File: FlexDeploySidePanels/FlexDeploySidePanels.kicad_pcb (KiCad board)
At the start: 2 copper layers, 411.4 x 215.5 mm, 0 parts

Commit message: added solar panels to layout
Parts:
- added H1: MountingHole_Pad, MountingHole:MountingHole_2.2mm_M2_DIN965_Pad_TopBottom, F.Cu at (839.4, 69.7)
- added H2: MountingHole_Pad, MountingHole:MountingHole_2.2mm_M2_DIN965_Pad_TopBottom, F.Cu at (839.4, 75.1)
- added H3: MountingHole_Pad, MountingHole:MountingHole_2.2mm_M2_DIN965_Pad_TopBottom, F.Cu at (839.4, 80.4)
- added H4: MountingHole_Pad, MountingHole:MountingHole_2.2mm_M2_DIN965_Pad_TopBottom, F.Cu at (839.4, 85.8)
- added SC1: ~, FlexDeploySidePanels:SM141K08TFV, F.Cu at (628.4, 82.2)
- added SC10: ~, FlexDeploySidePanels:SM141K08TFV, F.Cu at (674.7, 112.5)
- added SC11: ~, FlexDeploySidePanels:SM141K08TFV, F.Cu at (674.7, 142.8)
- added SC12: ~, FlexDeploySidePanels:SM141K08TFV, F.Cu at (674.7, 173.1)
- added SC13: ~, FlexDeploySidePanels:SM141K08TFV, F.Cu at (674.7, 203.4)
- added SC14: ~, FlexDeploySidePanels:SM141K08TFV, F.Cu at (674.7, 233.7)
- added SC15: ~, FlexDeploySidePanels:SM141K08TFV, F.Cu at (674.7, 264.0)
- added SC16: ~, FlexDeploySidePanels:SM141K08TFV, F.Cu at (674.7, 294.3)
- added SC17: ~, FlexDeploySidePanels:SM141K08TFV, F.Cu at (721.0, 82.2)
- added SC18: ~, FlexDeploySidePanels:SM141K08TFV, F.Cu at (721.0, 112.5)
- added SC19: ~, FlexDeploySidePanels:SM141K08TFV, F.Cu at (721.0, 142.8)
- added SC2: ~, FlexDeploySidePanels:SM141K08TFV, F.Cu at (628.4, 112.5)
- added SC20: ~, FlexDeploySidePanels:SM141K08TFV, F.Cu at (721.0, 173.1)
- added SC21: ~, FlexDeploySidePanels:SM141K08TFV, F.Cu at (721.0, 203.4)
- added SC22: ~, FlexDeploySidePanels:SM141K08TFV, F.Cu at (721.0, 233.7)
- added SC23: ~, FlexDeploySidePanels:SM141K08TFV, F.Cu at (721.0, 264.0)
- added SC24: ~, FlexDeploySidePanels:SM141K08TFV, F.Cu at (721.0, 294.3)
- added SC25: ~, FlexDeploySidePanels:SM141K08TFV, F.Cu at (767.3, 82.2)
- added SC26: ~, FlexDeploySidePanels:SM141K08TFV, F.Cu at (767.3, 112.5)
- added SC27: ~, FlexDeploySidePanels:SM141K08TFV, F.Cu at (767.3, 142.8)
- added SC28: ~, FlexDeploySidePanels:SM141K08TFV, F.Cu at (767.3, 173.1)
- added SC29: ~, FlexDeploySidePanels:SM141K08TFV, F.Cu at (767.3, 203.4)
- added SC3: ~, FlexDeploySidePanels:SM141K08TFV, F.Cu at (628.4, 142.8)
- added SC30: ~, FlexDeploySidePanels:SM141K08TFV, F.Cu at (767.3, 233.7)
- added SC31: ~, FlexDeploySidePanels:SM141K08TFV, F.Cu at (767.3, 264.0)
- added SC32: ~, FlexDeploySidePanels:SM141K08TFV, F.Cu at (767.3, 294.3)
- added SC33: ~, FlexDeploySidePanels:SM141K08TFV, F.Cu at (813.6, 82.2)
- added SC34: ~, FlexDeploySidePanels:SM141K08TFV, F.Cu at (813.6, 112.5)
- added SC35: ~, FlexDeploySidePanels:SM141K08TFV, F.Cu at (813.6, 142.8)
- added SC36: ~, FlexDeploySidePanels:SM141K08TFV, F.Cu at (813.6, 173.1)
- added SC37: ~, FlexDeploySidePanels:SM141K08TFV, F.Cu at (813.6, 203.4)
- added SC38: ~, FlexDeploySidePanels:SM141K08TFV, F.Cu at (813.6, 233.7)
- added SC4: ~, FlexDeploySidePanels:SM141K08TFV, F.Cu at (628.4, 173.1)
- added SC5: ~, FlexDeploySidePanels:SM141K08TFV, F.Cu at (628.4, 203.4)
- added SC6: ~, FlexDeploySidePanels:SM141K08TFV, F.Cu at (628.4, 233.7)
- added SC7: ~, FlexDeploySidePanels:SM141K08TFV, F.Cu at (628.4, 264.0)
- added SC8: ~, FlexDeploySidePanels:SM141K08TFV, F.Cu at (628.4, 294.3)
- added SC9: ~, FlexDeploySidePanels:SM141K08TFV, F.Cu at (674.7, 82.2)

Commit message: updated edge cuts
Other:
- board outline removed

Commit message: First rev of the full schematic and layout (very rough)
My traces are shit bc I don't know how to draw traces properly.
I didn't do the diode traces because I was struggling with vias.
The diodes should probably be moved bc I wasn't sure where was best to place them for ideal trace drawing.
I think we should have multiple traces of vsolar and gnd that cross each of the bends.
Multiple traces instead of one large one to prevent crack propagation. Better yet: multiple large ones.
Any copper in the bends should run perpendicular to the bending axis per manufacturer recommendations.
I made through hole pads for the mounting holes, but didn't place them in the right spots in the layout. The mounting holes are not at nice intervals in the CAD for good reason, but the kicad grid snap wasn't cutting it.
The cells are also not precisely placed. They are like +-2 mm or so, but they don't all line up perfectly which must change, for I am seriously irked by it. Now I know why nobody's board holes line up properly: they just put them in random spots near where they should be :skull:. Is there a way to position components by offsetting it from things by a float value (like dimension tool in CAD)?
Each panel has 8 cells in series. All panels are in parallel. We might find out from testing that we need to remove another cell from the body-fixed panel for the camera to freely glide out. In this case, we can put 9 cells on another panel :shrug::skin-tone-6:.
The camera mounting holes are in the edge cuts. Should these be through holes only? I am figuring we mount the camera on top of the pcb, and put screws through it, instead of cutting out a large rectangle for the camera to mount straight to the aluminum.
As I wrote that, I realized we will need places for the bolt heads on the other side.
The pcb mounting holes in the corners are also in the edge cuts.
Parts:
- added H10: MountingHole_Pad, MountingHole:MountingHole_2.2mm_M2_DIN965_Pad_TopBottom, F.Cu at (328.5, 88.5)
- added H11: MountingHole_Pad, MountingHole:MountingHole_2.2mm_M2_DIN965_Pad_TopBottom, F.Cu at (255.5, 91.5)
- added H12: MountingHole_Pad, MountingHole:MountingHole_2.2mm_M2_DIN965_Pad_TopBottom, F.Cu at (256.5, 328.5)
- added H13: MountingHole_Pad, MountingHole:MountingHole_2.2mm_M2_DIN965_Pad_TopBottom, F.Cu at (247.5, 329.0)
- added H14: MountingHole_Pad, MountingHole:MountingHole_2.2mm_M2_DIN965_Pad_TopBottom, F.Cu at (247.0, 91.5)
- added H15: MountingHole_Pad, MountingHole:MountingHole_2.2mm_M2_DIN965_Pad_TopBottom, F.Cu at (175.5, 90.5)
- added H16: MountingHole_Pad, MountingHole:MountingHole_2.2mm_M2_DIN965_Pad_TopBottom, F.Cu at (176.0, 323.5)
- added H17: MountingHole_Pad, MountingHole:MountingHole_2.2mm_M2_DIN965_Pad_TopBottom, F.Cu at (169.0, 325.0)
- added H18: MountingHole_Pad, MountingHole:MountingHole_2.2mm_M2_DIN965_Pad_TopBottom, F.Cu at (168.5, 91.0)
- added H19: MountingHole_Pad, MountingHole:MountingHole_2.2mm_M2_DIN965_Pad_TopBottom, F.Cu at (91.5, 91.0)
- added H20: MountingHole_Pad, MountingHole:MountingHole_2.2mm_M2_DIN965_Pad_TopBottom, F.Cu at (91.5, 194.0)
- added H21: MountingHole_Pad, MountingHole:MountingHole_2.2mm_M2_DIN965_Pad_TopBottom, F.Cu at (92.0, 323.0)
- added H5: MountingHole_Pad, MountingHole:MountingHole_2.2mm_M2_DIN965_Pad_TopBottom, F.Cu at (413.5, 322.0)
- added H6: MountingHole_Pad, MountingHole:MountingHole_2.2mm_M2_DIN965_Pad_TopBottom, F.Cu at (412.0, 90.5)
- added H7: MountingHole_Pad, MountingHole:MountingHole_2.2mm_M2_DIN965_Pad_TopBottom, F.Cu at (341.5, 90.0)
- added H8: MountingHole_Pad, MountingHole:MountingHole_2.2mm_M2_DIN965_Pad_TopBottom, F.Cu at (342.0, 325.5)
- added H9: MountingHole_Pad, MountingHole:MountingHole_2.2mm_M2_DIN965_Pad_TopBottom, F.Cu at (329.0, 324.5)
- added SC39: ~, FlexDeploySidePanels:SM141K08TFV, F.Cu at (147.0, 168.5)
- added SC40: ~, FlexDeploySidePanels:SM141K08TFV, F.Cu at (147.0, 214.5)
- added TP1: Testpoint, MountingHole:MountingHole_2.2mm_M2_DIN965_Pad_TopBottom, F.Cu at (128.5, 131.5)
- added TP2: Testpoint, MountingHole:MountingHole_2.2mm_M2_DIN965_Pad_TopBottom, F.Cu at (128.5, 137.5)
- added U1: CUS10S30, FlexDeploySidePanels:CUS10S30, F.Cu at (485.0, 261.0)
- added U10: CUS10S30, FlexDeploySidePanels:CUS10S30, F.Cu at (353.5, 243.6)
- added U11: CUS10S30, FlexDeploySidePanels:CUS10S30, F.Cu at (353.5, 246.7)
- added U12: CUS10S30, FlexDeploySidePanels:CUS10S30, F.Cu at (353.5, 249.9)
- added U13: CUS10S30, FlexDeploySidePanels:CUS10S30, F.Cu at (353.5, 253.0)
- added U14: CUS10S30, FlexDeploySidePanels:CUS10S30, F.Cu at (353.5, 256.1)
- added U15: CUS10S30, FlexDeploySidePanels:CUS10S30, F.Cu at (353.5, 259.2)
- added U16: CUS10S30, FlexDeploySidePanels:CUS10S30, F.Cu at (353.5, 262.3)
- added U17: CUS10S30, FlexDeploySidePanels:CUS10S30, F.Cu at (281.8, 262.2)
- added U18: CUS10S30, FlexDeploySidePanels:CUS10S30, F.Cu at (284.9, 262.2)
- added U19: CUS10S30, FlexDeploySidePanels:CUS10S30, F.Cu at (288.0, 262.2)
- added U2: CUS10S30, FlexDeploySidePanels:CUS10S30, F.Cu at (485.0, 205.0)
- added U20: CUS10S30, FlexDeploySidePanels:CUS10S30, F.Cu at (291.1, 262.2)
- added U21: CUS10S30, FlexDeploySidePanels:CUS10S30, F.Cu at (294.2, 262.2)
- added U22: CUS10S30, FlexDeploySidePanels:CUS10S30, F.Cu at (297.4, 262.2)
- added U23: CUS10S30, FlexDeploySidePanels:CUS10S30, F.Cu at (300.5, 262.2)
- added U24: CUS10S30, FlexDeploySidePanels:CUS10S30, F.Cu at (303.6, 262.2)
- added U25: CUS10S30, FlexDeploySidePanels:CUS10S30, F.Cu at (203.0, 262.2)
- added U26: CUS10S30, FlexDeploySidePanels:CUS10S30, F.Cu at (206.1, 262.2)
- added U27: CUS10S30, FlexDeploySidePanels:CUS10S30, F.Cu at (209.2, 262.2)
- added U28: CUS10S30, FlexDeploySidePanels:CUS10S30, F.Cu at (212.4, 262.2)
- added U29: CUS10S30, FlexDeploySidePanels:CUS10S30, F.Cu at (215.5, 262.2)
- added U3: CUS10S30, FlexDeploySidePanels:CUS10S30, F.Cu at (485.0, 151.5)
- added U30: CUS10S30, FlexDeploySidePanels:CUS10S30, F.Cu at (218.6, 262.2)
- added U31: CUS10S30, FlexDeploySidePanels:CUS10S30, F.Cu at (221.7, 262.2)
- added U32: CUS10S30, FlexDeploySidePanels:CUS10S30, F.Cu at (224.8, 262.2)
- added U33: CUS10S30, FlexDeploySidePanels:CUS10S30, F.Cu at (154.0, 262.6)
- added U34: CUS10S30, FlexDeploySidePanels:CUS10S30, F.Cu at (154.0, 259.5)
- added U35: CUS10S30, FlexDeploySidePanels:CUS10S30, F.Cu at (154.0, 256.4)
- added U36: CUS10S30, FlexDeploySidePanels:CUS10S30, F.Cu at (154.0, 253.3)
- added U37: CUS10S30, FlexDeploySidePanels:CUS10S30, F.Cu at (154.0, 250.1)
- added U38: CUS10S30, FlexDeploySidePanels:CUS10S30, F.Cu at (154.0, 247.0)
- added U39: CUS10S30, FlexDeploySidePanels:CUS10S30, F.Cu at (154.0, 243.9)
- added U4: CUS10S30, FlexDeploySidePanels:CUS10S30, F.Cu at (463.5, 151.5)
- added U40: CUS10S30, FlexDeploySidePanels:CUS10S30, F.Cu at (154.0, 240.8)
- added U5: CUS10S30, FlexDeploySidePanels:CUS10S30, F.Cu at (440.0, 151.5)
- added U6: CUS10S30, FlexDeploySidePanels:CUS10S30, F.Cu at (441.0, 205.0)
- added U7: CUS10S30, FlexDeploySidePanels:CUS10S30, F.Cu at (440.5, 260.8)
- added U8: CUS10S30, FlexDeploySidePanels:CUS10S30, F.Cu at (453.5, 260.8)
- added U9: CUS10S30, FlexDeploySidePanels:CUS10S30, F.Cu at (353.5, 240.5)
- moved SC33 733.5 mm to (110.0, 289.5), turned to -90 degrees
- moved SC34 709.5 mm to (118.0, 252.0)
- moved SC37 707.8 mm to (110.5, 122.5), turned to -90 degrees
- moved SC35 706.8 mm to (110.5, 214.5), turned to -90 degrees
- moved SC36 703.1 mm to (110.5, 168.5), turned to -90 degrees
- moved SC38 675.8 mm to (147.0, 122.5), turned to 90 degrees
- moved SC25 606.5 mm to (197.0, 288.5), turned to -90 degrees
- moved SC26 583.4 mm to (197.0, 235.5), turned to -90 degrees
- moved SC28 572.3 mm to (197.0, 126.0), turned to -90 degrees
- moved SC27 571.6 mm to (197.0, 181.0), turned to -90 degrees
- moved SC29 545.3 mm to (227.5, 126.0), turned to 90 degrees
- moved SC30 542.4 mm to (227.5, 181.0), turned to 90 degrees
- moved SC31 540.6 mm to (227.5, 235.5), turned to 90 degrees
- moved SC32 539.9 mm to (227.5, 288.5), turned to 90 degrees
- moved SC17 488.9 mm to (278.0, 289.0), turned to -90 degrees
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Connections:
- SC1 pad 1: (no net) -> Net-(SC1-+)
- SC10 pad 1: (no net) -> Net-(SC10-+)
- SC11 pad 1: (no net) -> Net-(SC10--)
- SC12 pad 1: (no net) -> Net-(SC11--)
- SC13 pad 1: (no net) -> Net-(SC12--)
- SC14 pad 1: (no net) -> Net-(SC13--)
- SC15 pad 1: (no net) -> Net-(SC14--)
- SC16 pad 1: (no net) -> Net-(SC15--)
- SC17 pad 1: (no net) -> VSOLAR
- SC18 pad 1: (no net) -> Net-(SC17--)
- SC19 pad 1: (no net) -> Net-(SC18--)
- SC2 pad 1: (no net) -> Net-(SC2-+)
- SC20 pad 1: (no net) -> Net-(SC19--)
- SC21 pad 1: (no net) -> Net-(SC20--)
- SC22 pad 1: (no net) -> Net-(SC21--)
- SC23 pad 1: (no net) -> Net-(SC22--)
- SC24 pad 1: (no net) -> Net-(SC23--)
- SC25 pad 1: (no net) -> VSOLAR
- SC26 pad 1: (no net) -> Net-(SC25--)
- SC27 pad 1: (no net) -> Net-(SC26--)
- SC28 pad 1: (no net) -> Net-(SC27--)
- SC29 pad 1: (no net) -> Net-(SC28--)
- SC3 pad 1: (no net) -> Net-(SC3-+)
- SC30 pad 1: (no net) -> Net-(SC29--)
- SC31 pad 1: (no net) -> Net-(SC30--)
- SC32 pad 1: (no net) -> Net-(SC31--)
- SC33 pad 1: (no net) -> VSOLAR
- SC34 pad 1: (no net) -> Net-(SC33--)
- SC35 pad 1: (no net) -> Net-(SC34--)
- SC36 pad 1: (no net) -> Net-(SC35--)
- SC37 pad 1: (no net) -> Net-(SC36--)
- SC38 pad 1: (no net) -> Net-(SC37--)
- SC4 pad 1: (no net) -> Net-(SC4-+)
- SC5 pad 1: (no net) -> Net-(SC5-+)
- SC6 pad 1: (no net) -> Net-(SC6-+)
- SC7 pad 1: (no net) -> Net-(SC7-+)
- SC8 pad 1: (no net) -> VSOLAR
- SC9 pad 1: (no net) -> VSOLAR
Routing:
- net VSOLAR: track 0.00 -> 1858.6 mm
- net Net-(SC4-+): track 0.00 -> 128.7 mm
- net Net-(SC15--): track 0.00 -> 84.1 mm
- net Net-(SC1-+): track 0.00 -> 76.0 mm
- net Net-(SC5-+): track 0.00 -> 72.7 mm
- net Net-(SC2-+): track 0.00 -> 71.5 mm
- net Net-(SC10-+): track 0.00 -> 59.9 mm
- net GND: track 0.00 -> 48.7 mm
- net Net-(SC3-+): track 0.00 -> 40.4 mm
- net Net-(SC7-+): track 0.00 -> 38.2 mm
- net Net-(SC37--): track 0.00 -> 36.5 mm
- net Net-(SC33--): track 0.00 -> 35.0 mm
- net Net-(SC12--): track 0.00 -> 33.7 mm
- net Net-(SC28--): track 0.00 -> 30.5 mm
- net Net-(SC20--): track 0.00 -> 29.0 mm
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
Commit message: style changes in schematic, moved board outline to Edge.Cuts layer, attempted routing to no avail
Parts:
- added U41: CUS10S30, FlexDeploySidePanels:CUS10S30, F.Cu at (67.3, 185.4)
- added U42: CUS10S30, FlexDeploySidePanels:CUS10S30, F.Cu at (67.3, 188.5)
- added U43: CUS10S30, FlexDeploySidePanels:CUS10S30, F.Cu at (361.9, 269.2)
- added U44: CUS10S30, FlexDeploySidePanels:CUS10S30, F.Cu at (67.3, 194.8)
- added U45: CUS10S30, FlexDeploySidePanels:CUS10S30, F.Cu at (442.0, 261.6)
- moved U13 50.4 mm to (402.6, 241.5)
- moved U14 50.3 mm to (402.6, 245.1)
- moved U15 49.2 mm to (402.6, 261.1)
- moved U16 49.2 mm to (402.6, 264.7), turned to 180 degrees
- moved U5 10.9 mm to (450.9, 152.8), turned to 180 degrees
- moved U7 10.4 mm to (450.9, 261.6), turned to 180 degrees
- moved U6 10.1 mm to (450.9, 207.2), turned to 180 degrees
- moved U8 9.04 mm to (444.5, 261.6)
- moved SC9 6.77 mm to (376.8, 251.5)
- moved U2 4.32 mm to (481.3, 207.2), turned to 180 degrees
- moved U3 3.88 mm to (481.3, 152.8), turned to 180 degrees
- moved U1 3.73 mm to (481.4, 261.8), turned to 180 degrees
- moved H1 3.51 mm to (504.2, 320.0)
- moved U9 2.10 mm to (351.8, 239.3)
- moved SC2 2.00 mm to (479.0, 234.5)
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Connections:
- SC17 pad 1: VSOLAR -> Net-(SC17-+)
- SC25 pad 1: VSOLAR -> Net-(SC25-+)
- SC33 pad 1: VSOLAR -> Net-(SC33-+)
- SC8 pad 1: VSOLAR -> Net-(SC8-+)
- SC9 pad 1: VSOLAR -> Net-(SC9-+)
- U17 pad 1: VSOLAR -> Net-(SC17-+)
- U25 pad 1: VSOLAR -> Net-(SC25-+)
- U33 pad 1: VSOLAR -> Net-(SC33-+)
- U8 pad 1: VSOLAR -> Net-(SC8-+)
- U9 pad 1: VSOLAR -> Net-(SC9-+)
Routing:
- net VSOLAR: track 1858.6 -> 0.00 mm
- net Net-(SC15--): track 84.1 -> 0.00 mm
- net Net-(SC10-+): track 59.9 -> 0.00 mm
- net Net-(SC8-+): track 0.00 -> 49.9 mm
- net Net-(SC4-+): track 128.7 -> 89.3 mm
- net Net-(SC6-+): track 25.8 -> 64.5 mm
- net Net-(SC37--): track 36.5 -> 0.00 mm
- net Net-(SC33--): track 35.0 -> 0.00 mm
- net Net-(SC28--): track 30.5 -> 0.00 mm
- net Net-(SC20--): track 29.0 -> 0.00 mm
- net Net-(SC34--): track 23.0 -> 0.00 mm
- net Net-(SC7-+): track 38.2 -> 20.5 mm
- net Net-(SC21--): track 16.5 -> 0.00 mm
- net Net-(SC19--): track 16.5 -> 0.00 mm
- net Net-(SC29--): track 16.0 -> 0.00 mm
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- added copper zone on B.Cu, net GND
- added copper zone on F.Cu, net VSOLAR
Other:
- board outline added: 414 x 215.5 mm

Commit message: routed diodes
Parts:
- U1, U10, U11, U12, U13, U14, U15, U16, U17, U18, U19, U2, U20, U21, U22, U23, U24, U25, U26, U27, U28, U29, U3, U30, U31, U32, U33, U34, U35, U36, U37, U38, U39, U4, U40, U41, U42, U43, U44, U45, U5, U6, U7, U8, U9: value CUS10S30 -> BAS70-02V-G3-08; footprint FlexDeploySidePanels:CUS10S30 -> FlexDeploySidePanels:BAS70-02V-G3-08
- moved U44 211.9 mm to (268.4, 261.6)
- moved U41 142.1 mm to (187.2, 261.6)
- moved U42 134.8 mm to (127.5, 309.1), turned to 180 degrees
- moved U37 130.6 mm to (127.8, 122.2), turned to 90 degrees
- moved U38 126.6 mm to (129.8, 122.8), turned to -90 degrees
- moved TP2 118.5 mm to (145.3, 254.8)
- moved TP1 111.6 mm to (145.0, 241.9)
- moved U28 110.3 mm to (198.8, 152.8), turned to 0 degrees
- moved U22 110.1 mm to (309.1, 152.8), turned to 0 degrees
- moved U20 110.1 mm to (279.9, 152.8), turned to 0 degrees
- moved U30 110.0 mm to (229.3, 152.8), turned to 0 degrees
- moved U29 109.5 mm to (213.3, 152.8), turned to 0 degrees
- moved U21 109.5 mm to (294.5, 152.8), turned to 0 degrees
- moved U36 89.0 mm to (127.8, 168.2), turned to 90 degrees
- moved U39 78.9 mm to (129.8, 168.8), turned to -90 degrees
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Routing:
- net Net-(SC12--): track 29.5 -> 241.0 mm, vias 0 -> 2
- net GND: track 48.2 -> 218.9 mm
- net Net-(SC11--): track 7.00 -> 116.2 mm
- net Net-(SC13--): track 7.00 -> 108.5 mm
- net Net-(SC28--): track 0.00 -> 90.7 mm
- net Net-(SC20--): track 0.00 -> 89.9 mm
- net Net-(SC37--): track 0.00 -> 88.2 mm
- net Net-(SC14--): track 0.00 -> 78.6 mm
- net Net-(SC34--): track 0.00 -> 65.7 mm
- net Net-(SC10--): track 0.00 -> 65.3 mm
- net Net-(SC23--): track 0.00 -> 64.5 mm
- net Net-(SC22--): track 0.00 -> 64.5 mm
- net Net-(SC19--): track 0.00 -> 64.2 mm
- net Net-(SC18--): track 0.00 -> 64.1 mm
- net Net-(SC26--): track 0.00 -> 64.0 mm
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- added copper zone on In1.Cu, net GND
- added copper zone on In2.Cu, net VSOLAR
- removed copper zone on B.Cu, net GND
- removed copper zone on F.Cu, net VSOLAR
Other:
- copper layers 2 -> 4

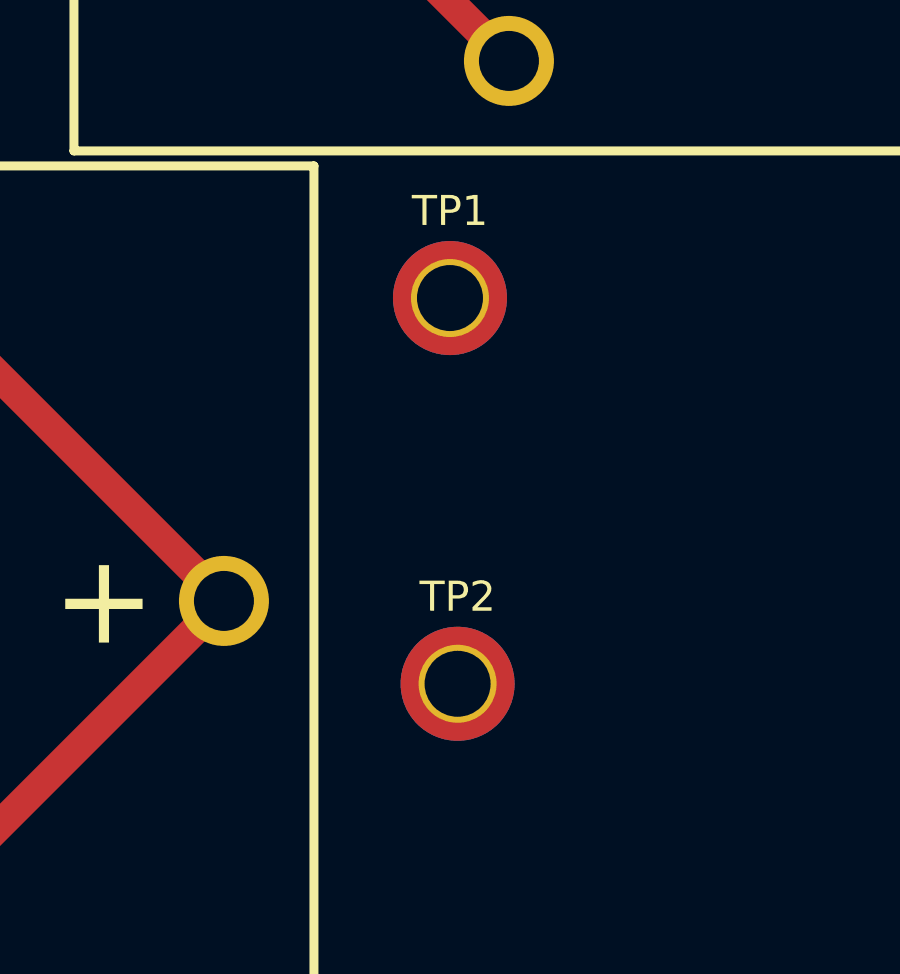
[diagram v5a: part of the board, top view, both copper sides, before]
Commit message: added 3d models
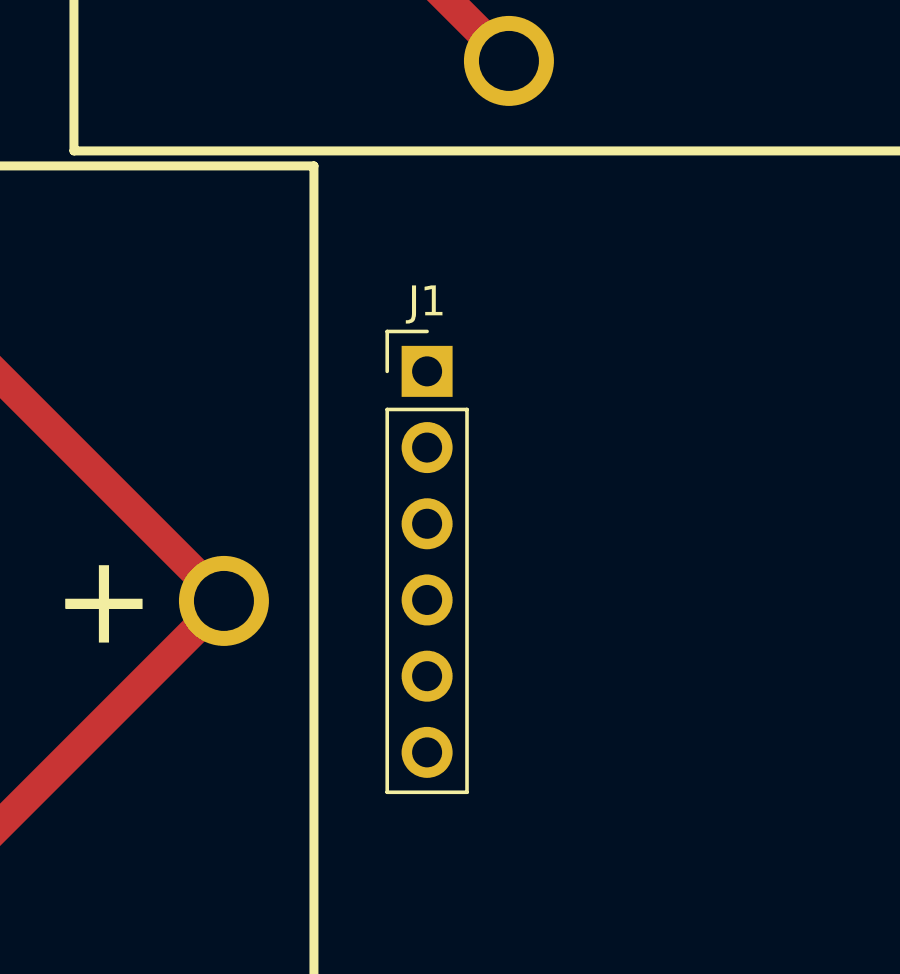
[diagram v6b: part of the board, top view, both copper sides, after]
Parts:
- removed TP1, TP2: Testpoint, MountingHole:MountingHole_2.2mm_M2_DIN965_Pad_TopBottom
- added J1: Through_Hole_1, Connector_PinHeader_2.54mm:PinHeader_1x06_P2.54mm_Vertical, F.Cu at (144.3, 244.3)

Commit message: centered connection hole
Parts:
- moved J1 46.4 mm to (128.8, 200.7)
- moved U35 3.94 mm to (127.8, 218.2)
- moved U40 3.38 mm to (129.8, 218.2)
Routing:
- net Net-(SC35--): track 58.7 -> 62.7 mm
- net Net-(SC39--): track 58.7 -> 62.1 mm
- net Net-(SC34--): track 65.7 -> 63.1 mm
- net GND: track 218.9 -> 216.8 mm
